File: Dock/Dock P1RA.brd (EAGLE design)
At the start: 50 x 40 mm, 14 parts, among them J2 MF-CON-2.54mm-01x07, J3 MF-CON-2.54mm-01x05, U1 MCP73831T-2ACI/OT

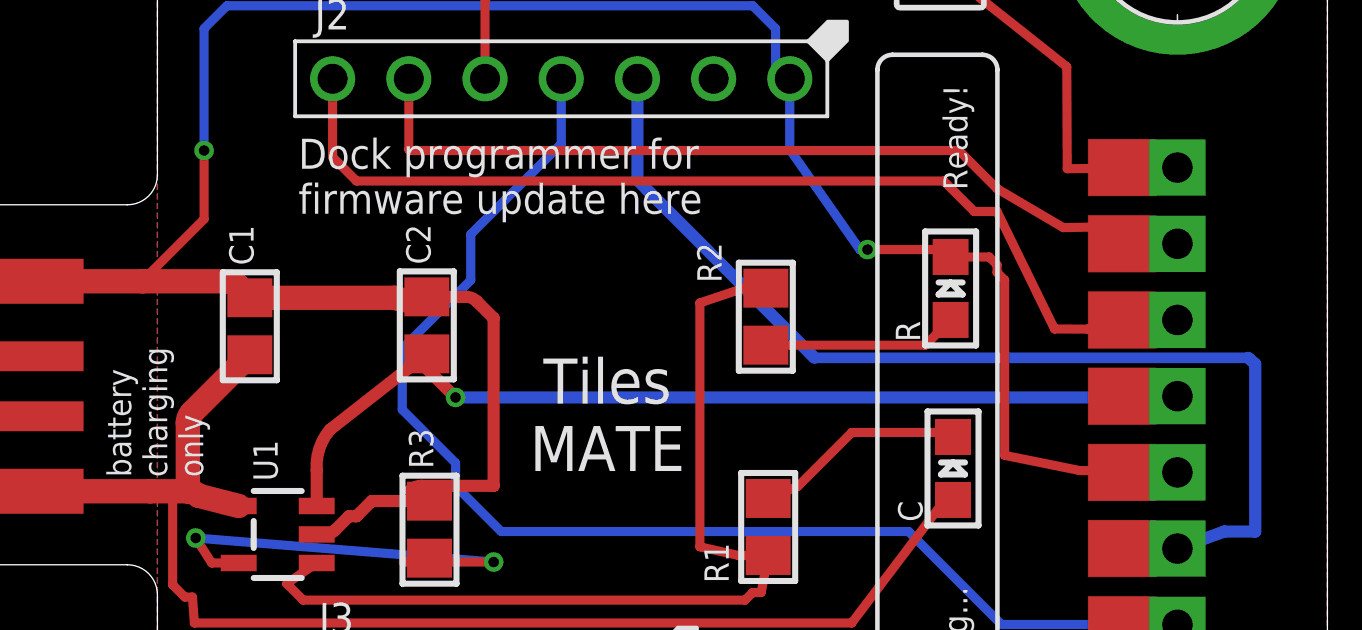
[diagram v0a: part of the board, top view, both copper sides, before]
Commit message: switched imu from LSM9DS1 to ADXL345
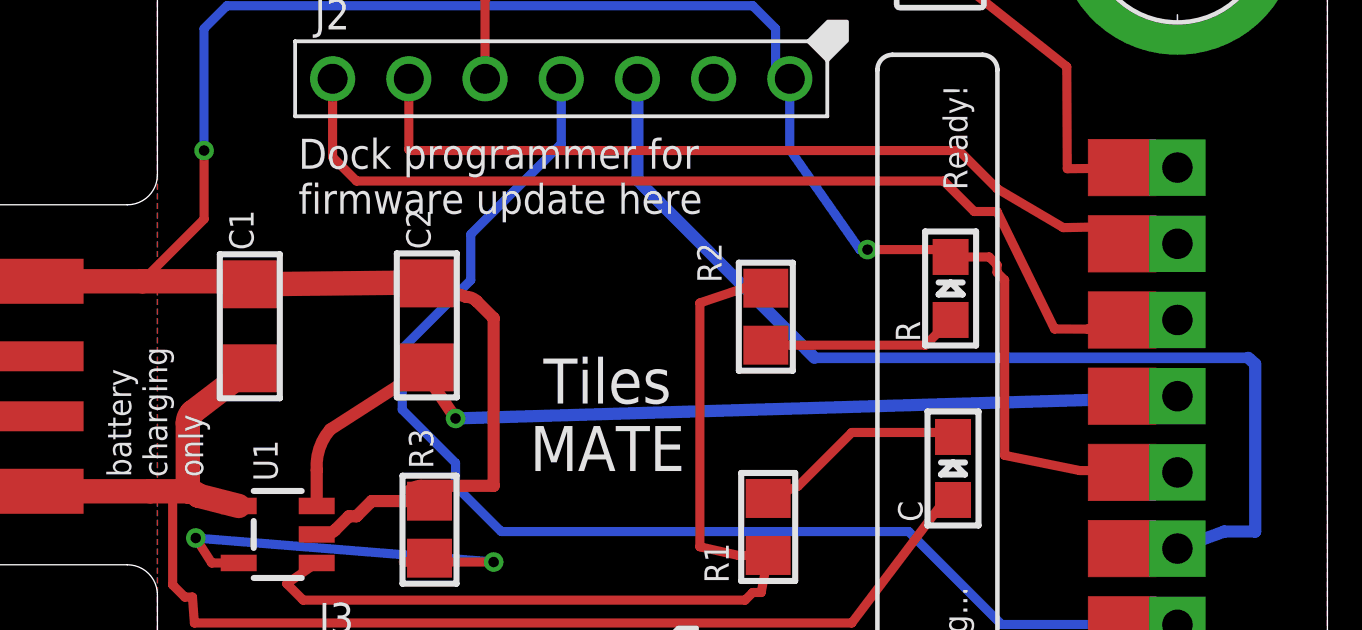
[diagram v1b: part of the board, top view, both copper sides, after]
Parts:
- C1, C2: device microbuilder:0805 -> microbuilder:1206
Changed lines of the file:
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@@
 </autorouter>
 <elements>
-<element name="C1" library="microbuilder" package="0805" value="10µF" x="4.08" y="-18.05" rot="R90"/>
-<element name="C2" library="microbuilder" package="0805" value="10µF" x="9.98" y="-18.02" rot="R90"/>
+<element name="C1" library="microbuilder" package="1206" value="10µF" x="4.08" y="-18.05" rot="R90"/>
+<element name="C2" library="microbuilder" package="1206" value="10µF" x="9.98" y="-18.02" rot="R90"/>
 <element name="CN1" library="microbuilder" package="USBA_PCB" value="" x="-5.01" y="-20.05" smashed="yes">
 <attribute name="VALUE" x="-10.09" y="-27.035" size="0.4064" layer="27" ratio="10"/>
@@
 <wire x1="0.508" y1="-16.55" x2="3.32289375" y2="-16.55" width="0.8128" layer="1"/>
 <wire x1="3.32289375" y1="-16.55" x2="3.676446875" y2="-16.696446875" width="0.8128" layer="1" curve="-45"/>
-<wire x1="3.676446875" y1="-16.696446875" x2="4.08" y2="-17.1" width="0.8128" layer="1"/>
-<wire x1="4.08" y1="-17.1" x2="8.907575" y2="-17.1" width="0.8128" layer="1"/>
-<wire x1="8.907575" y1="-17.1" x2="9.98" y2="-17.07" width="0.8128" layer="1" curve="45"/>
-<wire x1="9.98" y1="-17.07" x2="11.29089375" y2="-17.07" width="0.4064" layer="1"/>
+<wire x1="3.676446875" y1="-16.696446875" x2="4.08" y2="-16.65" width="0.8128" layer="1"/>
+<wire x1="4.08" y1="-16.65" x2="9.007575" y2="-16.6" width="0.8128" layer="1"/>
+<wire x1="9.007575" y1="-16.6" x2="9.98" y2="-16.62" width="0.8128" layer="1" curve="45"/>
+<wire x1="9.98" y1="-16.62" x2="11.29089375" y2="-17.07" width="0.4064" layer="1"/>
 <wire x1="11.29089375" y1="-17.07" x2="11.644446875" y2="-17.216446875" width="0.4064" layer="1" curve="-45"/>
 <wire x1="11.644446875" y1="-17.216446875" x2="12.208" y2="-17.78" width="0.4064" layer="1"/>
@@
 <wire x1="2.01279375" y1="-23.55" x2="2.01279375" y2="-21.2743125" width="0.8128" layer="1"/>
 <wire x1="2.01279375" y1="-21.2743125" x2="2.159240625" y2="-20.920759375" width="0.8128" layer="1" curve="-45"/>
-<wire x1="2.159240625" y1="-20.920759375" x2="4.08" y2="-19" width="0.8128" layer="1"/>
+<wire x1="2.159240625" y1="-20.920759375" x2="4.08" y2="-19.45" width="0.8128" layer="1"/>
 <wire x1="27.52" y1="-23.84" x2="27.246" y2="-23.84" width="0.3048" layer="1"/>
 <wire x1="27.246" y1="-23.84" x2="24.146" y2="-27.94" width="0.3048" layer="1"/>
@@
 <wire x1="6.3101" y1="-24.04" x2="6.3101" y2="-22.84700625" width="0.4064" layer="1"/>
 <wire x1="6.3101" y1="-22.84700625" x2="6.756546875" y2="-21.493453125" width="0.4064" layer="1" curve="-45"/>
-<wire x1="6.756546875" y1="-21.493453125" x2="9.98" y2="-18.97" width="0.4064" layer="1"/>
-<wire x1="9.98" y1="-18.97" x2="9.4864" y2="-18.97" width="0.4064" layer="1"/>
-<wire x1="9.4864" y1="-18.97" x2="10.938" y2="-20.4216" width="0.4064" layer="1"/>
-<via x="10.938" y="-20.4216" extent="1-16" drill="0.35"/>
-<wire x1="10.938" y1="-20.4216" x2="34.9484" y2="-20.4216" width="0.4064" layer="16"/>
+<wire x1="6.756546875" y1="-21.493453125" x2="9.98" y2="-19.42" width="0.4064" layer="1"/>
+<wire x1="9.98" y1="-19.42" x2="9.4864" y2="-18.97" width="0.4064" layer="1"/>
+<wire x1="9.4864" y1="-18.97" x2="10.938" y2="-21.1216" width="0.4064" layer="1"/>
+<via x="10.938" y="-21.1216" extent="1-16" drill="0.35"/>
+<wire x1="10.938" y1="-21.1216" x2="34.9484" y2="-20.4216" width="0.4064" layer="16"/>
 <wire x1="34.9484" y1="-20.4216" x2="35" y2="-20.38" width="0.4064" layer="16"/>
 </signal>
